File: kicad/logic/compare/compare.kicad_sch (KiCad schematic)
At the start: 9 parts

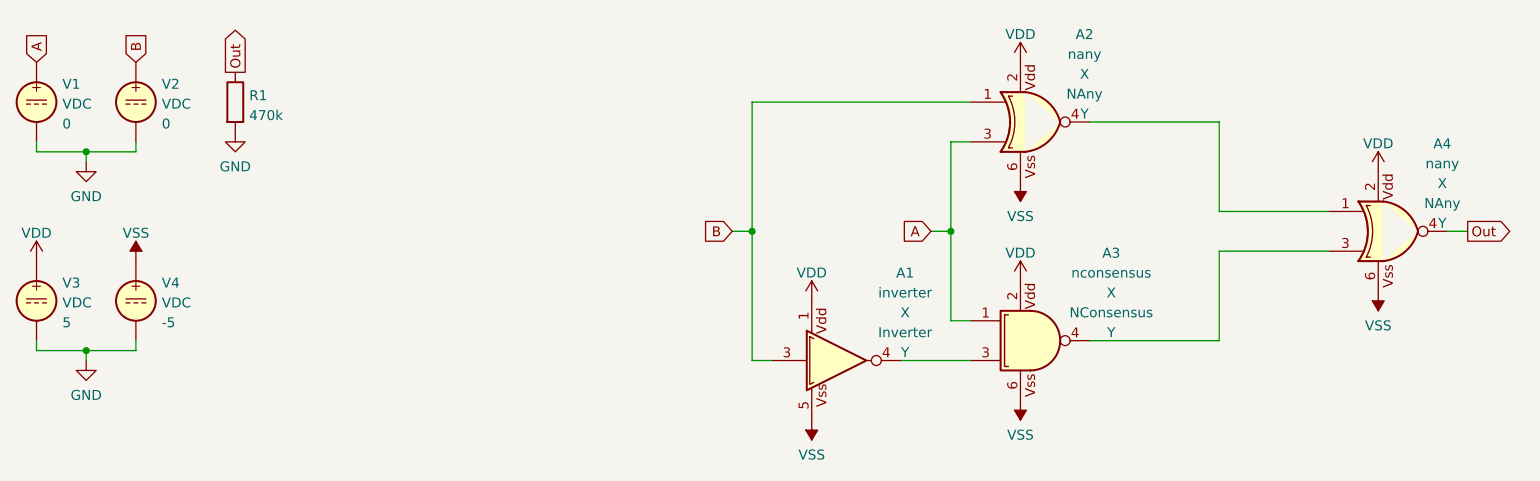
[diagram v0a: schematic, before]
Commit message: update to kicad 9
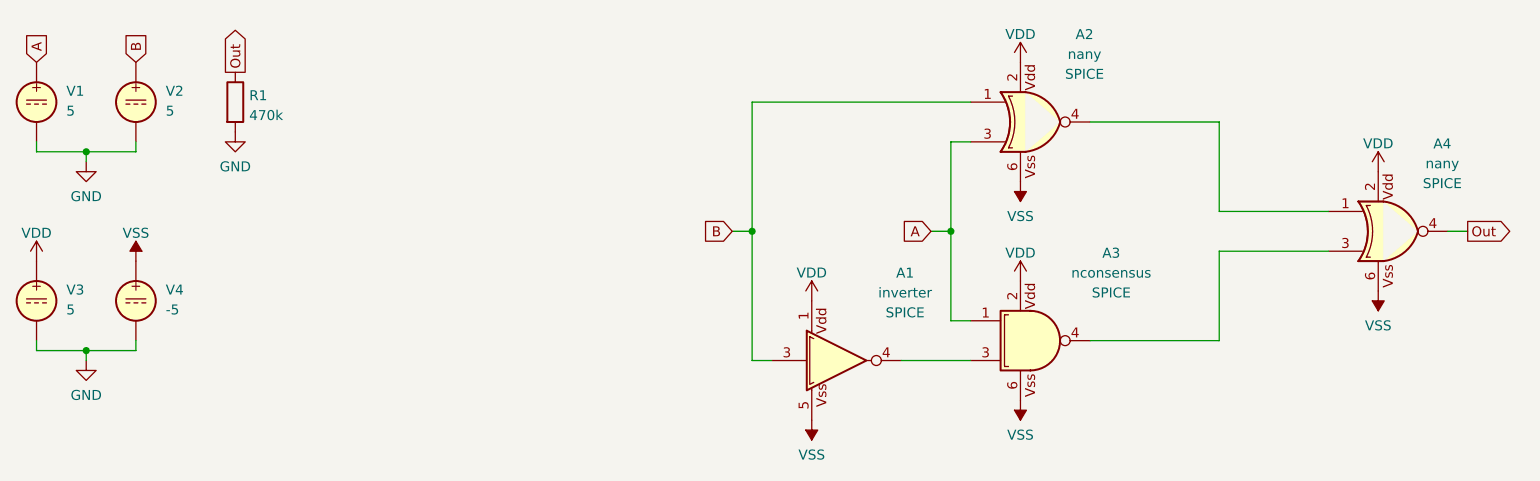
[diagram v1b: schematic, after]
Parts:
- A1: Spice_Lib_File ${TRITIUM_LIB}/TritiumSpice.lib -> (none); Spice_Model Inverter -> (none); Spice_Netlist_Enabled Y -> (none); Spice_Primitive X -> (none)
- A2, A4: Spice_Lib_File ${TRITIUM_LIB}/TritiumSpice.lib -> (none); Spice_Model NAny -> (none); Spice_Netlist_Enabled Y -> (none); Spice_Primitive X -> (none)
- A3: Spice_Lib_File ${TRITIUM_LIB}/TritiumSpice.lib -> (none); Spice_Model NConsensus -> (none); Spice_Netlist_Enabled Y -> (none); Spice_Primitive X -> (none)
- V1, V2: value VDC -> 5; Spice_Model 0 -> (none); Spice_Netlist_Enabled Y -> (none); Spice_Primitive V -> (none)
- V3: value VDC -> 5; Spice_Model 5 -> (none); Spice_Netlist_Enabled Y -> (none); Spice_Primitive V -> (none)
- V4: value VDC -> -5; Spice_Model -5 -> (none); Spice_Netlist_Enabled Y -> (none); Spice_Primitive V -> (none)
